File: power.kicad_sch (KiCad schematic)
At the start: 139 parts, among them J3 Conn_01x01, J4 Conn_01x01, U1 CSD95472Q5MC, U16 CSD95472Q5MC, U3 TPS53647, U36 MCP1824T-1202E, U4 CSD95472Q5MC, U5 CSD95472Q5MC, U6 AP3211, U7 MCP1824T-0802E

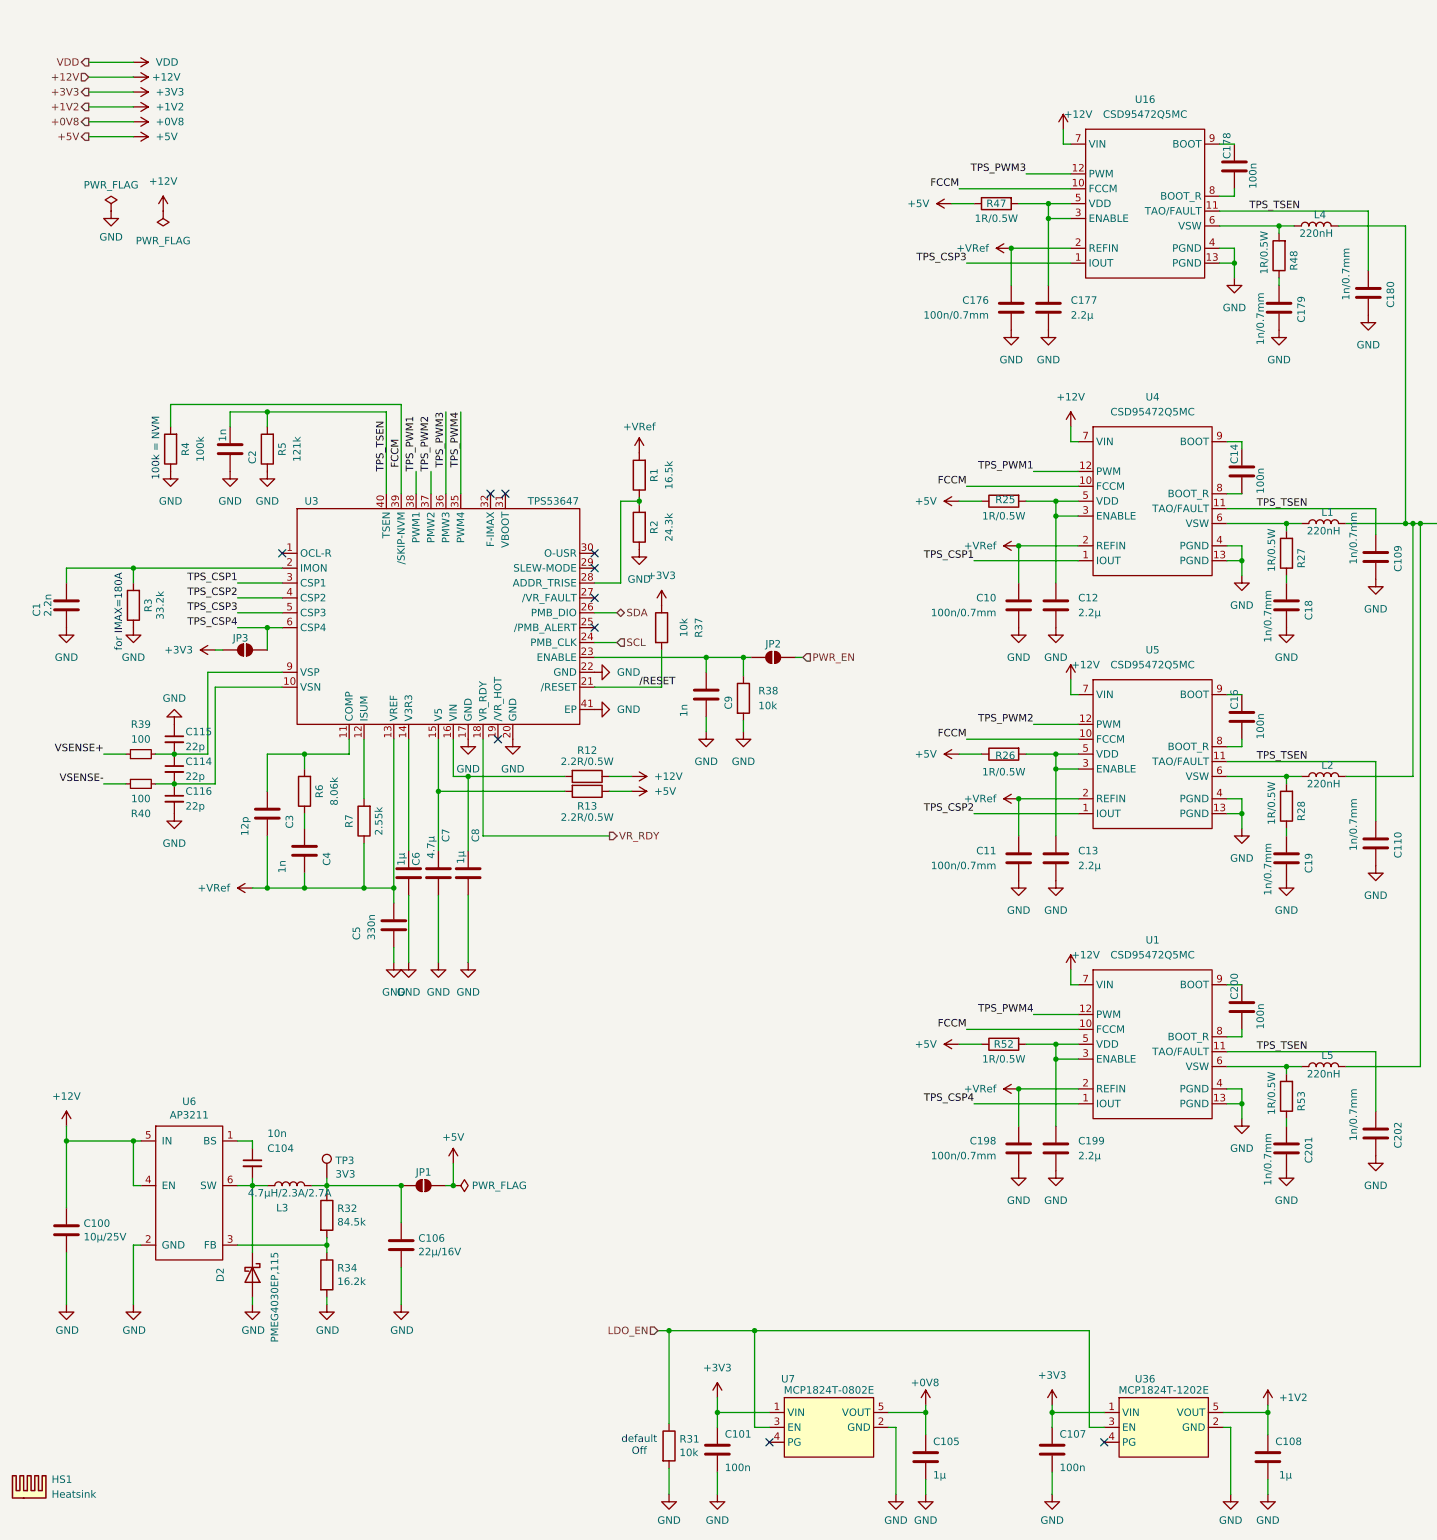
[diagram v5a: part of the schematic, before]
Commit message: BOM changes
1nF  to 1nF 0.7mm etc
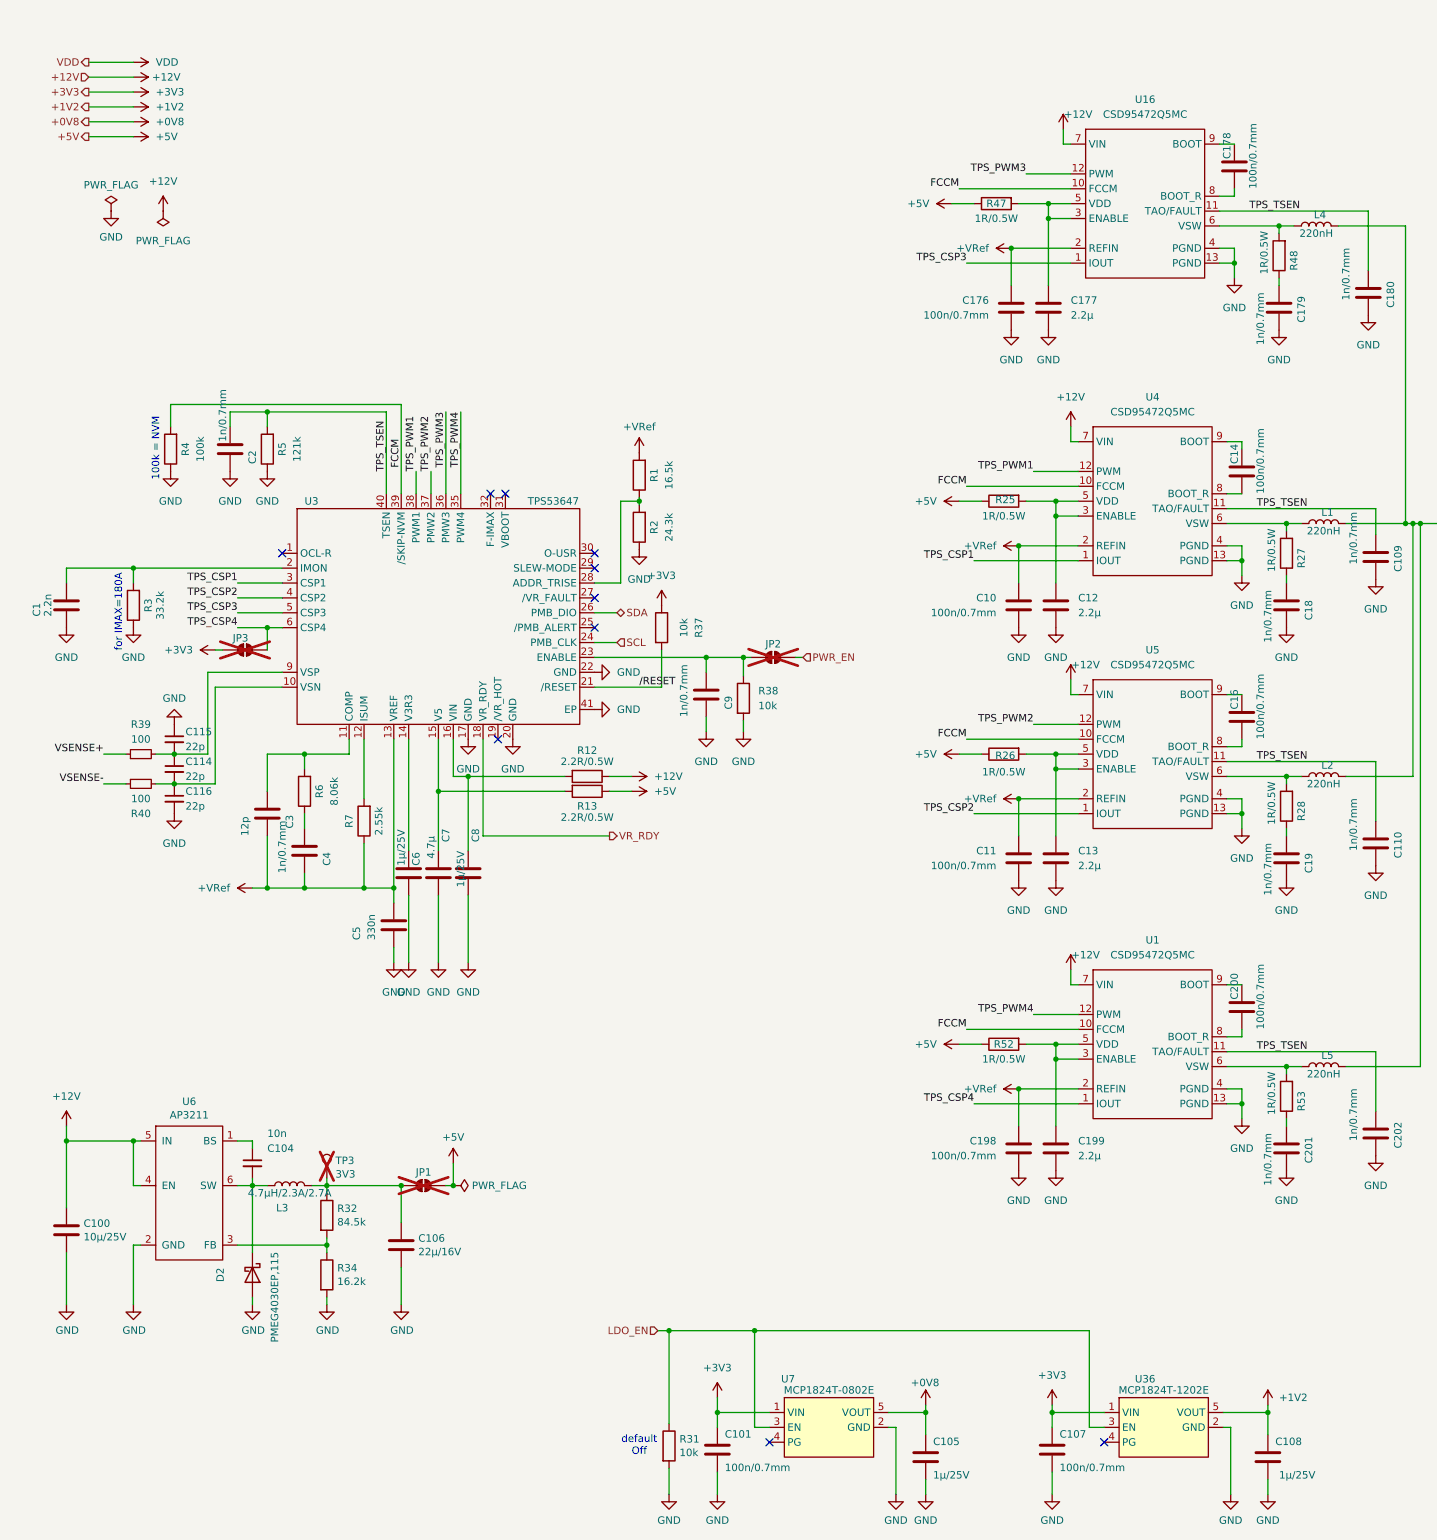
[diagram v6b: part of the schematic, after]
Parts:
- removed HS1: Heatsink, symbol Mechanical:Heatsink
- C1: Distributor (none) -> D; Manufacturer (none) -> CL21C222JBFNNNE; OrderNr (none) -> 1276-2993-1-ND
- C101, C107, C14, C16, C178, C200: value 100n -> 100n/0.7mm; Distributor (none) -> D; Manufacturer (none) -> AC0805KRX7R9BB104; OrderNr (none) -> 311-3037-1-ND
- C104: Distributor (none) -> D; Manufacturer (none) -> 885012207011; OrderNr (none) -> 732-8021-1-ND
- C105, C108, C6, C8: value 1µ -> 1µ/25V; Distributor (none) -> D; Manufacturer (none) -> CL21B105KAFNNNE; OrderNr (none) -> 1276-1066-1-ND
- C106: Distributor (none) -> D; Manufacturer (none) -> CL31A226MOCLNNC; OrderNr (none) -> 1276-2728-1-ND
- C112, C117, C181, C215: Manufacturer (none) -> GRM2165C2A332JA01D
- C113, C118, C182, C216: Distributor (none) -> D; Manufacturer (none) -> CL21B105KAFNNNE; OrderNr (none) -> 1276-1066-1-ND
- C114, C115, C116: Distributor (none) -> D; Manufacturer (none) -> KGM15ACG1H220JT; OrderNr (none) -> 478-KGM15ACG1H220JTCT-ND
- C12, C13, C177, C199: Distributor (none) -> D; Manufacturer (none) -> CL21A225KAFNNNG; OrderNr (none) -> 1276-6458-1-ND
- C2, C4, C9: value 1n -> 1n/0.7mm; Distributor (none) -> D; Manufacturer (none) -> CC0805KRX7R0BB102; OrderNr (none) -> 311-1472-1-ND
- C3: Manufacturer (none) -> KGM15ACG2A120JM
- C5: Distributor (none) -> D; Manufacturer (none) -> C0805C334K3RECAUTO; OrderNr (none) -> 399-C0805C334K3RECAUTOCT-ND
- C7: Distributor (none) -> D; Manufacturer (none) -> CL21A475KAQNNNE; OrderNr (none) -> 1276-1244-1-ND
- JP1, JP2, JP3, TP3: now not fitted
- L5: footprint Qaxe:IFLR-4031GC-01-8x10 -> myfootprints:IFLR-4031GC-01-8x10
- R1: Manufacturer (none) -> CRCW080516K5FKEA
- R2: Manufacturer (none) -> RC0805FR-0724K3L
- R29, R30: Distributor (none) -> D; Manufacturer (none) -> RMCF0805ZT0R00; OrderNr (none) -> RMCF0805ZT0R00CT-ND
- R3: Manufacturer (none) -> RMCF0805FT33K2
- R31, R37, R38: Distributor (none) -> D; Manufacturer (none) -> RMCF0805FT10K0; OrderNr (none) -> RMCF0805FT10K0CT-ND
- R32: Distributor (none) -> D; Manufacturer (none) -> RC0805FR-0784K5L; OrderNr (none) -> 311-84.5KCRCT-ND
- R34: Manufacturer (none) -> RMCF0805FT16K2
- R39, R40: Distributor (none) -> D; Manufacturer (none) -> RC0805FR-07100RL; OrderNr (none) -> 311-100CRCT-ND
- R4: Distributor (none) -> D; Manufacturer (none) -> RMCF0805FT100K; OrderNr (none) -> RMCF0805FT100KCT-ND
- R5: Manufacturer (none) -> RMCF0805FT121K
- R6: Distributor (none) -> D; Manufacturer (none) -> RMCF0805FT8K06; OrderNr (none) -> RMCF0805FT8K06CT-ND
- R7: Manufacturer (none) -> RC0805FR-072K55L

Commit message: 0502
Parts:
- removed JP3: Disable Phase 4, Jumper:SolderJumper-2_P1.3mm_Open_RoundedPad1.0x1.5mm, symbol Jumper:SolderJumper_2_Open
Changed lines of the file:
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@@
 	)
 	(junction
-		(at 62.23 123.19)
-		(diameter 0)
-		(color 0 0 0 0)
-	)
-	(junction
 		(at 354.33 120.65)
 		(diameter 0)
@@
 	(wire
 		(pts
-			(xy 53.34 127) (xy 54.61 127)
-		)
-		(stroke
-			(width 0)
-			(type default)
-		)
-	)
-	(wire
-		(pts
 			(xy 190.5 50.8) (xy 195.58 50.8)
 		)
@@
 	(wire
 		(pts
-			(xy 57.15 123.19) (xy 62.23 123.19)
+			(xy 57.15 123.19) (xy 64.77 123.19)
 		)
 		(stroke
@@
 	(wire
 		(pts
-			(xy 62.23 127) (xy 62.23 123.19)
-		)
-		(stroke
-			(width 0)
-			(type default)
-		)
-	)
-	(wire
-		(pts
 			(xy 43.18 149.86) (xy 46.355 149.86)
 		)
@@
 	(wire
 		(pts
-			(xy 62.23 123.19) (xy 64.77 123.19)
-		)
-		(stroke
-			(width 0)
-			(type default)
-		)
-	)
-	(wire
-		(pts
 			(xy 311.15 116.84) (xy 311.15 120.65)
 		)
@@
 	)
 	(symbol
-		(lib_id "Jumper:SolderJumper_2_Open")
-		(at 58.42 127 0)
-		(unit 1)
-		(exclude_from_sim yes)
-		(in_bom no)
-		(on_board yes)
-		(dnp yes)
-		(property "Reference" "JP3"
-			(at 57.658 124.968 0)
-			(effects
-				(font
-					(size 1.27 1.27)
-				)
-			)
-		)
-		(property "Value" "Disable Phase 4"
-			(at 55.372 129.032 0)
-			(effects
-				(font
-					(size 1.27 1.27)
-				)
-				(hide yes)
-			)
-		)
-		(property "Footprint" "Jumper:SolderJumper-2_P1.3mm_Open_RoundedPad1.0x1.5mm"
-			(at 58.42 127 0)
-			(effects
-				(font
-					(size 1.27 1.27)
-				)
-				(hide yes)
-			)
-		)
-		(property "Datasheet" "~"
-			(at 58.42 127 0)
-			(effects
-				(font
-					(size 1.27 1.27)
-				)
-				(hide yes)
-			)
-		)
-		(property "Description" "Solder Jumper, 2-pole, open"
-			(at 58.42 127 0)
-			(effects
-				(font
-					(size 1.27 1.27)
-				)
-				(hide yes)
-			)
-		)
-		(pin "2"
-		)
-		(pin "1"
-		)
-		(instances
-			(project "Nerd8"
-				(path "/e63e39d7-6ac0-4ffd-8aa3-1841a4541b55/8ec0a9c6-2b78-44ef-a83d-9047d2828409"
-					(reference "JP3")
-					(unit 1)
-				)
-			)
-		)
-	)
-	(symbol
 		(lib_id "Device:C")
 		(at 195.58 68.58 0)
@@
 					(unit 1)
 				)
-			)
-		)
-	)
-	(symbol
-		(lib_name "+3V3_2")
-		(lib_id "power:+3V3")
-		(at 53.34 127 90)
-		(unit 1)
-		(exclude_from_sim no)
-		(in_bom yes)
-		(on_board yes)
-		(dnp no)
-		(fields_autoplaced yes)
-		(property "Reference" "#PWR0363"
-			(at 57.15 127 0)
-			(effects
-				(font
-					(size 1.27 1.27)
-				)
-				(hide yes)
-			)
-		)
-		(property "Value" "+3V3"
-			(at 49.53 126.9999 90)
-			(effects
-				(font
-					(size 1.27 1.27)
-				)
-				(justify left)
-			)
-		)
-		(property "Footprint" ""
-			(at 53.34 127 0)
-			(effects
-				(font
-					(size 1.27 1.27)
-				)
-				(hide yes)
-			)
-		)
-		(property "Datasheet" ""
-			(at 53.34 127 0)
-			(effects
-				(font
-					(size 1.27 1.27)
-				)
-				(hide yes)
-			)
-		)
-		(property "Description" "Power symbol creates a global label with name \"+3V3\""
-			(at 53.34 127 0)
-			(effects
-				(font
-					(size 1.27 1.27)
-				)
-				(hide yes)
-			)
-		)
-		(pin "1"
-		)
-		(instances
-			(project "Nerd8"
-				(path "/e63e39d7-6ac0-4ffd-8aa3-1841a4541b55/8ec0a9c6-2b78-44ef-a83d-9047d2828409"
-					(reference "#PWR0363")
-					(unit 1)
-				)
